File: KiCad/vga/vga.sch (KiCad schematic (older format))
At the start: 0 parts

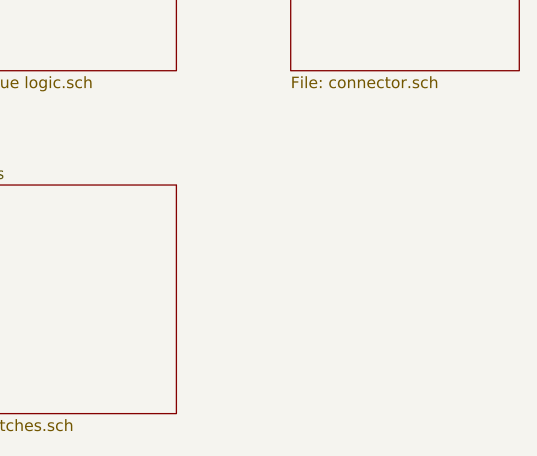
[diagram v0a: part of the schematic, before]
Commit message: Replaced MAX7000 CPLD with MAX II in graphics adapter. PCB redesign with smaller size.
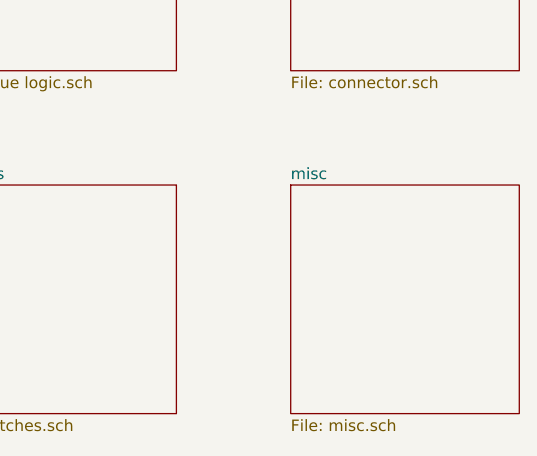
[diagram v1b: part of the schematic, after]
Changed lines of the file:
@@
 $Descr A4 11693 8268
 encoding utf-8
-Sheet 1 6
+Sheet 1 7
 Title ""
 Date ""
@@
 F1 "connector.sch" 50
 $EndSheet
+$Sheet
+S 4000 2500 1000 1000
+U 5FB0F245
+F0 "misc" 50
+F1 "misc.sch" 50
+$EndSheet
 $EndSCHEMATC
